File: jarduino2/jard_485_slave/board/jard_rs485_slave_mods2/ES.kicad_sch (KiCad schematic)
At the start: 29 parts, among them U1 BPC_Mod485

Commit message: Modification titre du schéma + Nomenclature
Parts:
- U1: Bpcref 1 -> (none)
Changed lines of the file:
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@@
       (effects (font (size 1.27 1.27)) hide)
     )
-    (property "Bpcref" "1" (at 173.99 67.175 0)
+    (property "Bpcref" "" (at 173.99 67.175 0)
       (effects (font (size 1.27 1.27)))
     )
+    (property "Description" "Module RS485 pour Arduino" (at 186.69 78.74 0)
+      (effects (font (size 1.27 1.27)) hide)
+    )
     (pin "1")

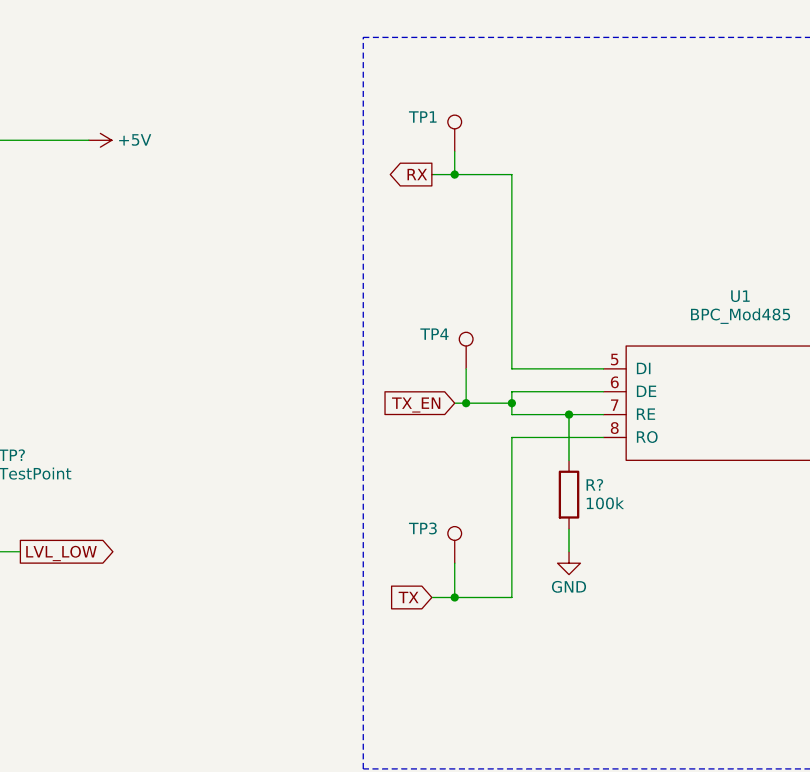
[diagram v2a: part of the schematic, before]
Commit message: Inversion RX/TX 485
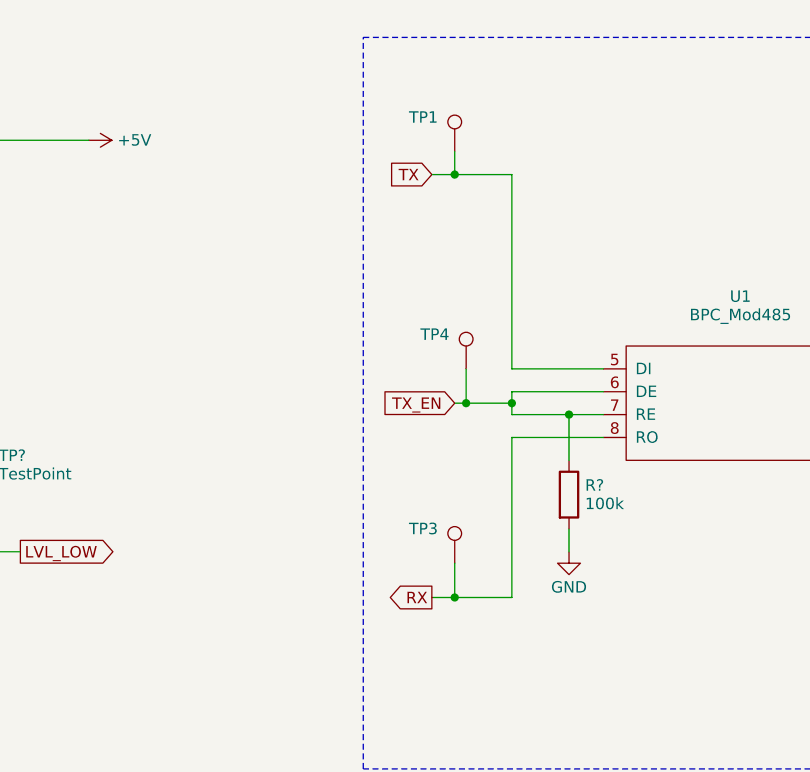
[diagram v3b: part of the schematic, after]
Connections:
- net RX: now also TP3.1, U1.8 (RO); no longer TP1.1, U1.5 (DI)
- net TX: now also TP1.1, U1.5 (DI); no longer TP3.1, U1.8 (RO)
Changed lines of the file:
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@@
   (title_block
     (title "Carte de commande d'un OYA - Esclave RS485")
-    (date "2024-04-27")
+    (date "2024-05-04")
     (rev "F0")
     (company "BPC")
@@
     (effects (font (size 1.27 1.27)) (justify left bottom))
   )
+  (global_label "TX" (shape input) (at 139.7 49.53 180) (fields_autoplaced)
+    (effects (font (size 1.27 1.27)) (justify right))
+    (property "Intersheetrefs" "${INTERSHEET_REFS}" (at 134.6171 49.53 0)
+      (effects (font (size 1.27 1.27)) (justify right) hide)
+    )
+  )
   (global_label "FLOW" (shape output) (at 81.28 43.18 0) (fields_autoplaced)
     (effects (font (size 1.27 1.27)) (justify left))
@@
     )
   )
-  (global_label "TX" (shape input) (at 139.7 96.52 180) (fields_autoplaced)
-    (effects (font (size 1.27 1.27)) (justify right))
-    (property "Intersheetrefs" "${INTERSHEET_REFS}" (at 134.6171 96.52 0)
-      (effects (font (size 1.27 1.27)) (justify right) hide)
-    )
-  )
-  (global_label "RX" (shape output) (at 139.7 49.53 180) (fields_autoplaced)
-    (effects (font (size 1.27 1.27)) (justify right))
-    (property "Intersheetrefs" "${INTERSHEET_REFS}" (at 134.3147 49.53 0)
-      (effects (font (size 1.27 1.27)) (justify right) hide)
-    )
-  )
   (global_label "POWER_12V" (shape input) (at 101.6 137.16 180) (fields_autoplaced)
     (effects (font (size 1.27 1.27)) (justify right))
@@
     )
   )
+  (global_label "RX" (shape output) (at 139.7 96.52 180) (fields_autoplaced)
+    (effects (font (size 1.27 1.27)) (justify right))
+    (property "Intersheetrefs" "${INTERSHEET_REFS}" (at 134.3147 96.52 0)
+      (effects (font (size 1.27 1.27)) (justify right) hide)
+    )
+  )
